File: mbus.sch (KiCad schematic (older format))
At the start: 17 parts, among them Q1 PN2222A, Q2 PN2222A, Q3 BC640, Q4 PN2222A

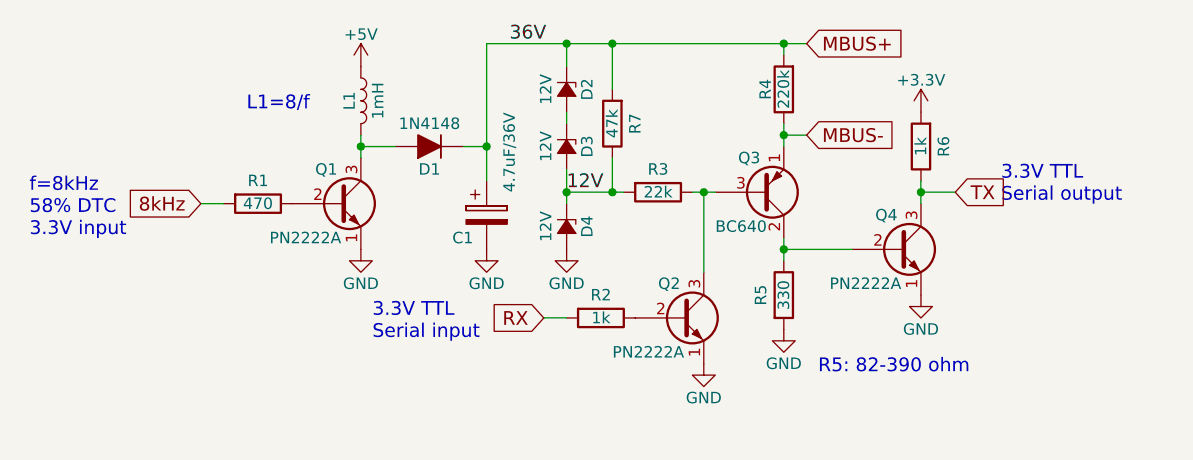
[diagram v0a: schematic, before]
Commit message: cosmetic changes (spacing)
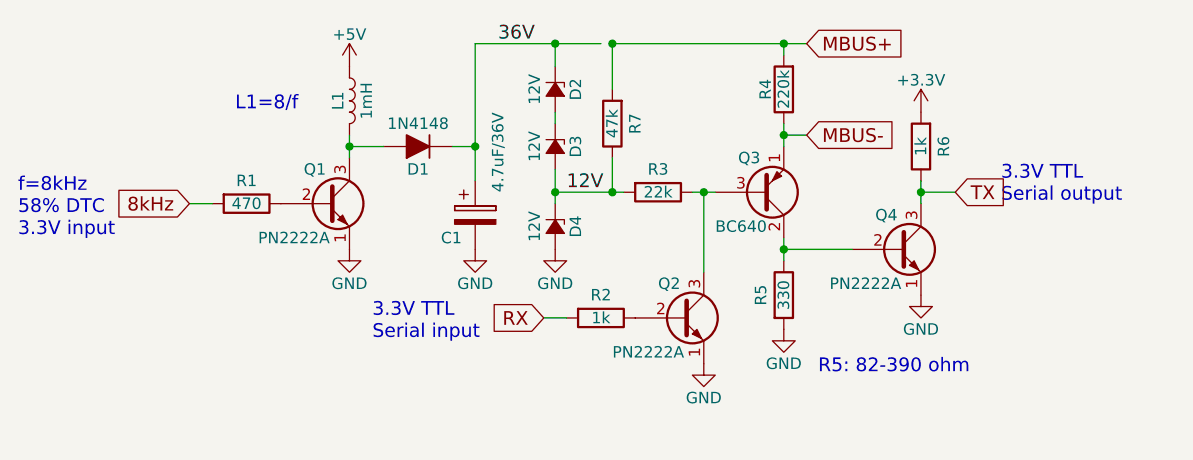
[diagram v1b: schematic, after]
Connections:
- wire segments 33 -> 23
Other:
- moved on the sheet: C1, D1, D2, D3, D4, L1, Q1, R1
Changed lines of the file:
@@
 L R R1
 U 1 1 59E32A7E
-P 2150 4300
-F 0 "R1" V 2050 4300 50  0000 C CNN
-F 1 "470" V 2150 4300 50  0000 C CNN
-F 2 "" V 2080 4300 50  0001 C CNN
-F 3 "" H 2150 4300 50  0001 C CNN
-	1    2150 4300
-	0    1    1    0
-$EndComp
-Wire Wire Line
-	2000 4300 1900 4300
+P 2100 4300
+F 0 "R1" V 2000 4300 50  0000 C CNN
+F 1 "470" V 2100 4300 50  0000 C CNN
+F 2 "" V 2030 4300 50  0001 C CNN
+F 3 "" H 2100 4300 50  0001 C CNN
+	1    2100 4300
+	0    1    1    0
+$EndComp
+Wire Wire Line
+	1950 4300 1850 4300
 $Comp
 L Q_NPN_EBC Q1
 U 1 1 59E32AF3
-P 2500 4300
-F 0 "Q1" H 2400 4450 50  0000 L CNN
-F 1 "PN2222A" H 2200 4150 50  0000 L CNN
-F 2 "" H 2700 4400 50  0001 C CNN
-F 3 "" H 2500 4300 50  0001 C CNN
-	1    2500 4300
+P 2450 4300
+F 0 "Q1" H 2350 4450 50  0000 L CNN
+F 1 "PN2222A" H 2150 4150 50  0000 L CNN
+F 2 "" H 2650 4400 50  0001 C CNN
+F 3 "" H 2450 4300 50  0001 C CNN
+	1    2450 4300
 	1    0    0    -1
 $EndComp
@@
 L GND #PWR2
 U 1 1 59E32B2F
-P 2600 4500
-F 0 "#PWR2" H 2600 4250 50  0001 C CNN
-F 1 "GND" H 2600 4350 50  0000 C CNN
-F 2 "" H 2600 4500 50  0001 C CNN
-F 3 "" H 2600 4500 50  0001 C CNN
-	1    2600 4500
+P 2550 4500
+F 0 "#PWR2" H 2550 4250 50  0001 C CNN
+F 1 "GND" H 2550 4350 50  0000 C CNN
+F 2 "" H 2550 4500 50  0001 C CNN
+F 3 "" H 2550 4500 50  0001 C CNN
+	1    2550 4500
 	1    0    0    -1
 $EndComp
@@
 L L L1
 U 1 1 59E32B47
-P 2600 3850
-F 0 "L1" V 2550 3850 50  0000 C CNN
-F 1 "1mH" V 2675 3850 50  0000 C CNN
-F 2 "" H 2600 3850 50  0001 C CNN
-F 3 "" H 2600 3850 50  0001 C CNN
-	1    2600 3850
-	1    0    0    -1
-$EndComp
-Wire Wire Line
-	2600 4000 2600 4050
-Wire Wire Line
-	2600 4050 2600 4100
+P 2550 3850
+F 0 "L1" V 2500 3850 50  0000 C CNN
+F 1 "1mH" V 2625 3850 50  0000 C CNN
+F 2 "" H 2550 3850 50  0001 C CNN
+F 3 "" H 2550 3850 50  0001 C CNN
+	1    2550 3850
+	1    0    0    -1
+$EndComp
+Wire Wire Line
+	2550 4000 2550 4100
 $Comp
 L +5V #PWR1
 U 1 1 59E32BAD
-P 2600 3700
-F 0 "#PWR1" H 2600 3550 50  0001 C CNN
-F 1 "+5V" H 2600 3840 50  0000 C CNN
-F 2 "" H 2600 3700 50  0001 C CNN
-F 3 "" H 2600 3700 50  0001 C CNN
-	1    2600 3700
+P 2550 3700
+F 0 "#PWR1" H 2550 3550 50  0001 C CNN
+F 1 "+5V" H 2550 3840 50  0000 C CNN
+F 2 "" H 2550 3700 50  0001 C CNN
+F 3 "" H 2550 3700 50  0001 C CNN
+	1    2550 3700
 	1    0    0    -1
 $EndComp
@@
 L D_ALT D1
 U 1 1 59E32BC7
-P 2900 4050
-F 0 "D1" H 2900 4150 50  0000 C CNN
-F 1 "1N4148" H 2900 3950 50  0000 C CNN
-F 2 "" H 2900 4050 50  0001 C CNN
-F 3 "" H 2900 4050 50  0001 C CNN
-	1    2900 4050
+P 2850 4050
+F 0 "D1" H 2850 4150 50  0000 C CNN
+F 1 "1N4148" H 2850 3950 50  0000 C CNN
+F 2 "" H 2850 4050 50  0001 C CNN
+F 3 "" H 2850 4050 50  0001 C CNN
+	1    2850 4050
 	-1   0    0    1
 $EndComp
 Wire Wire Line
-	2750 4050 2600 4050
-Connection ~ 2600 4050
+	2700 4050 2550 4050
+Connection ~ 2550 4050
 $Comp
 L D_Zener_Small_ALT D4
 U 1 1 59E32C36
-P 3500 4400
-F 0 "D4" H 3500 4490 50  0000 C CNN
-F 1 "12V" H 3500 4310 50  0000 C CNN
-F 2 "" V 3500 4400 50  0001 C CNN
-F 3 "" V 3500 4400 50  0001 C CNN
-	1    3500 4400
+P 3450 4400
+F 0 "D4" H 3450 4490 50  0000 C CNN
+F 1 "12V" H 3450 4310 50  0000 C CNN
+F 2 "" V 3450 4400 50  0001 C CNN
+F 3 "" V 3450 4400 50  0001 C CNN
+	1    3450 4400
 	0    1    1    0
 $EndComp
@@
 L D_Zener_Small_ALT D3
 U 1 1 59E32CBA
-P 3500 4050
-F 0 "D3" H 3500 4140 50  0000 C CNN
-F 1 "12V" H 3500 3960 50  0000 C CNN
-F 2 "" V 3500 4050 50  0001 C CNN
-F 3 "" V 3500 4050 50  0001 C CNN
-	1    3500 4050
+P 3450 4050
+F 0 "D3" H 3450 4140 50  0000 C CNN
+F 1 "12V" H 3450 3960 50  0000 C CNN
+F 2 "" V 3450 4050 50  0001 C CNN
+F 3 "" V 3450 4050 50  0001 C CNN
+	1    3450 4050
 	0    1    1    0
 $EndComp
@@
 L D_Zener_Small_ALT D2
 U 1 1 59E32D01
-P 3500 3800
-F 0 "D2" H 3500 3890 50  0000 C CNN
-F 1 "12V" H 3500 3710 50  0000 C CNN
-F 2 "" V 3500 3800 50  0001 C CNN
-F 3 "" V 3500 3800 50  0001 C CNN
-	1    3500 3800
+P 3450 3800
+F 0 "D2" H 3450 3890 50  0000 C CNN
+F 1 "12V" H 3450 3710 50  0000 C CNN
+F 2 "" V 3450 3800 50  0001 C CNN
+F 3 "" V 3450 3800 50  0001 C CNN
+	1    3450 3800
 	0    1    1    0
 $EndComp
@@
 L GND #PWR4
 U 1 1 59E32D8F
-P 3500 4500
-F 0 "#PWR4" H 3500 4250 50  0001 C CNN
-F 1 "GND" H 3500 4350 50  0000 C CNN
-F 2 "" H 3500 4500 50  0001 C CNN
-F 3 "" H 3500 4500 50  0001 C CNN
-	1    3500 4500
-	1    0    0    -1
-$EndComp
-Wire Wire Line
-	3500 4150 3500 4250
-Wire Wire Line
-	3500 4250 3500 4300
-Wire Wire Line
-	3500 3950 3500 3900
+P 3450 4500
+F 0 "#PWR4" H 3450 4250 50  0001 C CNN
+F 1 "GND" H 3450 4350 50  0000 C CNN
+F 2 "" H 3450 4500 50  0001 C CNN
+F 3 "" H 3450 4500 50  0001 C CNN
+	1    3450 4500
+	1    0    0    -1
+$EndComp
+Wire Wire Line
+	3450 4150 3450 4300
+Wire Wire Line
+	3450 3950 3450 3900
 $Comp
 L CP C1
 U 1 1 59E32EFA
-P 3150 4350
-F 0 "C1" H 3000 4250 50  0000 L CNN
-F 1 "4.7uF/36V" V 3250 4450 50  0000 L CNN
-F 2 "" H 3188 4200 50  0001 C CNN
-F 3 "" H 3150 4350 50  0001 C CNN
-	1    3150 4350
-	1    0    0    -1
-$EndComp
-Wire Wire Line
-	3150 3600 3150 4050
-Wire Wire Line
-	3150 4050 3150 4200
-Wire Wire Line
-	3150 3600 3500 3600
-Wire Wire Line
-	3500 3600 3700 3600
-Wire Wire Line
-	3700 3600 4450 3600
-Wire Wire Line
-	4450 3600 4550 3600
-Wire Wire Line
-	3500 3600 3500 3700
-Wire Wire Line
-	3050 4050 3150 4050
-Connection ~ 3150 4050
+P 3100 4350
+F 0 "C1" H 2950 4250 50  0000 L CNN
+F 1 "4.7uF/36V" V 3200 4450 50  0000 L CNN
+F 2 "" H 3138 4200 50  0001 C CNN
+F 3 "" H 3100 4350 50  0001 C CNN
+	1    3100 4350
+	1    0    0    -1
+$EndComp
+Wire Wire Line
+	3100 3600 3100 4200
+Wire Wire Line
+	3100 3600 3650 3600
+Wire Wire Line
+	3700 3600 4550 3600
+Wire Wire Line
+	3450 3600 3450 3700
+Wire Wire Line
+	3000 4050 3100 4050
+Connection ~ 3100 4050
 $Comp
 L GND #PWR3
 U 1 1 59E32FEB
-P 3150 4500
-F 0 "#PWR3" H 3150 4250 50  0001 C CNN
-F 1 "GND" H 3150 4350 50  0000 C CNN
-F 2 "" H 3150 4500 50  0001 C CNN
-F 3 "" H 3150 4500 50  0001 C CNN
-	1    3150 4500
+P 3100 4500
+F 0 "#PWR3" H 3100 4250 50  0001 C CNN
+F 1 "GND" H 3100 4350 50  0000 C CNN
+F 2 "" H 3100 4500 50  0001 C CNN
+F 3 "" H 3100 4500 50  0001 C CNN
+	1    3100 4500
 	1    0    0    -1
 $EndComp
@@
 $EndComp
 Wire Wire Line
-	3500 4250 3700 4250
-Wire Wire Line
-	3700 4250 3750 4250
-Connection ~ 3500 4250
+	3450 4250 3750 4250
+Connection ~ 3450 4250
 Text Label 3500 4250 0    60   ~ 0
 12V
-Text Label 3250 3600 0    60   ~ 0
+Text Label 3200 3600 0    60   ~ 0
 36V
 $Comp
@@
 $EndComp
 Wire Wire Line
-	4050 4250 4100 4250
-Wire Wire Line
-	4100 4250 4150 4250
+	4050 4250 4150 4250
 $Comp
 L Q_NPN_EBC Q2
@@
 Wire Wire Line
 	4450 3600 4450 3650
-Connection ~ 3500 3600
-Wire Wire Line
-	4450 3950 4450 4000
-Wire Wire Line
-	4450 4000 4450 4050
+Connection ~ 3450 3600
+Wire Wire Line
+	4450 3950 4450 4050
 $Comp
 L R R5
@@
 $EndComp
 Wire Wire Line
-	4450 4450 4450 4500
-Wire Wire Line
-	4450 4500 4450 4550
+	4450 4450 4450 4550
 $Comp
 L Q_NPN_EBC Q4
@@
 $EndComp
 Wire Wire Line
-	5050 4200 5050 4250
-Wire Wire Line
-	5050 4250 5050 4300
+	5050 4200 5050 4300
 Wire Wire Line
 	5050 4250 5200 4250
@@
 Text GLabel 5200 4250 2    60   Input ~ 0
 TX
-Text GLabel 1900 4300 0    60   Input ~ 0
+Text GLabel 1850 4300 0    60   Input ~ 0
 8kHz
 Text Notes 5400 4300 0    60   ~ 0
@@
 Text Notes 2650 4900 0    60   ~ 0
 3.3V TTL\nSerial input
-Text Notes 1150 4450 0    60   ~ 0
+Text Notes 1100 4450 0    60   ~ 0
 f=8kHz \n58% DTC\n3.3V input
 Text Notes 4600 5050 0    60   ~ 0
 R5: 82-390 ohm
-Text Notes 2100 3900 0    60   ~ 0
+Text Notes 2050 3900 0    60   ~ 0
 L1=8/f
 $Comp

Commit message: larger input resistor R2=15k
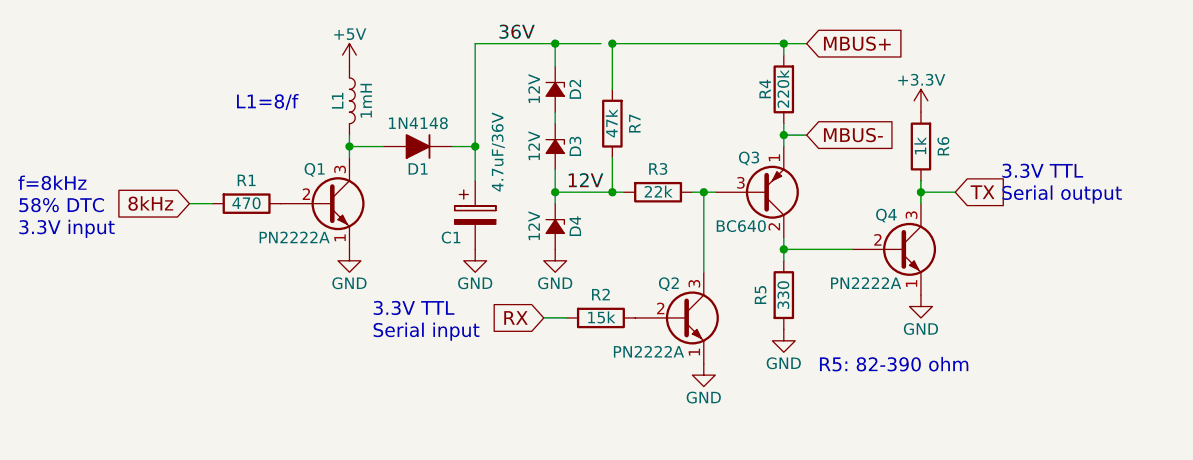
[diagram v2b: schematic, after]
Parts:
- R2: value 1k -> 15k
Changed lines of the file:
@@
 P 3650 4800
 F 0 "R2" V 3550 4800 50  0000 C CNN
-F 1 "1k" V 3650 4800 50  0000 C CNN
+F 1 "15k" V 3650 4800 50  0000 C CNN
 F 2 "" V 3580 4800 50  0001 C CNN
 F 3 "" H 3650 4800 50  0001 C CNN

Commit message: Pullup on RX and pic update
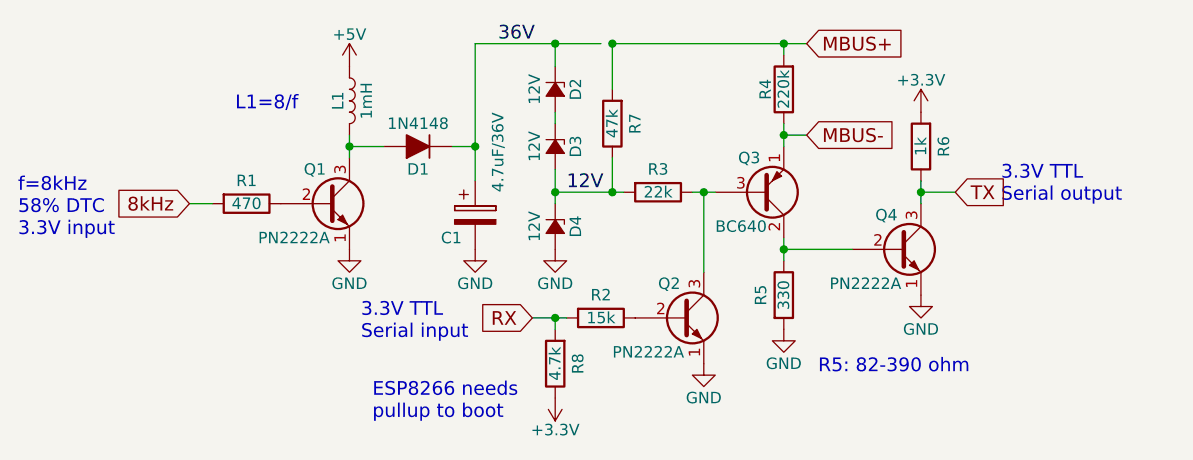
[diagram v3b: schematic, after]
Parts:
- added R8: 4.7k, symbol R
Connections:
- wire segments 23 -> 24
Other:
- note added: "ESP8266 needs\npullup to boot"
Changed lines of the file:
@@
 Connection ~ 4100 4250
 $Comp
-L GND #PWR5
+L GND #PWR6
 U 1 1 59E33748
 P 4100 5000
-F 0 "#PWR5" H 4100 4750 50  0001 C CNN
+F 0 "#PWR6" H 4100 4750 50  0001 C CNN
 F 1 "GND" H 4100 4850 50  0000 C CNN
 F 2 "" H 4100 5000 50  0001 C CNN
@@
 $EndComp
 Wire Wire Line
-	3500 4800 3400 4800
+	3500 4800 3350 4800
 $Comp
 L R R4
@@
 $EndComp
 $Comp
-L GND #PWR6
+L GND #PWR7
 U 1 1 59E33DF2
 P 4450 4850
-F 0 "#PWR6" H 4450 4600 50  0001 C CNN
+F 0 "#PWR7" H 4450 4600 50  0001 C CNN
 F 1 "GND" H 4450 4700 50  0000 C CNN
 F 2 "" H 4450 4850 50  0001 C CNN
@@
 Connection ~ 4450 4500
 $Comp
-L GND #PWR8
+L GND #PWR9
 U 1 1 59E34040
 P 5050 4700
-F 0 "#PWR8" H 5050 4450 50  0001 C CNN
+F 0 "#PWR9" H 5050 4450 50  0001 C CNN
 F 1 "GND" H 5050 4550 50  0000 C CNN
 F 2 "" H 5050 4700 50  0001 C CNN
@@
 	4450 4000 4550 4000
 Connection ~ 4450 4000
-Text GLabel 3400 4800 0    60   Input ~ 0
+Text GLabel 3350 4800 0    60   Input ~ 0
 RX
 Text GLabel 5200 4250 2    60   Input ~ 0
@@
 Text Notes 5400 4300 0    60   ~ 0
 3.3V TTL\nSerial output
-Text Notes 2650 4900 0    60   ~ 0
+Text Notes 2600 4900 0    60   ~ 0
 3.3V TTL\nSerial input
 Text Notes 1100 4450 0    60   ~ 0
@@
 L1=8/f
 $Comp
-L +3.3V #PWR?
+L +3.3V #PWR8
 U 1 1 59E48729
 P 5050 3900
-F 0 "#PWR?" H 5050 3750 50  0001 C CNN
+F 0 "#PWR8" H 5050 3750 50  0001 C CNN
 F 1 "+3.3V" H 5050 4040 50  0000 C CNN
 F 2 "" H 5050 3900 50  0001 C CNN
@@
 	1    0    0    -1
 $EndComp
+$Comp
+L R R8
+U 1 1 59E73425
+P 3450 5000
+F 0 "R8" V 3350 5000 50  0000 C CNN
+F 1 "4.7k" V 3450 5000 50  0000 C CNN
+F 2 "" V 3380 5000 50  0001 C CNN
+F 3 "" H 3450 5000 50  0001 C CNN
+	1    3450 5000
+	-1   0    0    1
+$EndComp
+Wire Wire Line
+	3450 4850 3450 4800
+Connection ~ 3450 4800
+$Comp
+L +3.3V #PWR5
+U 1 1 59E7355E
+P 3450 5150
+F 0 "#PWR5" H 3450 5000 50  0001 C CNN
+F 1 "+3.3V" H 3450 5290 50  0000 C CNN
+F 2 "" H 3450 5150 50  0001 C CNN
+F 3 "" H 3450 5150 50  0001 C CNN
+	1    3450 5150
+	-1   0    0    1
+$EndComp
+Text Notes 2650 5250 0    60   ~ 0
+ESP8266 needs\npullup to boot
 $EndSCHEMATC

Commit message: connect 36V line
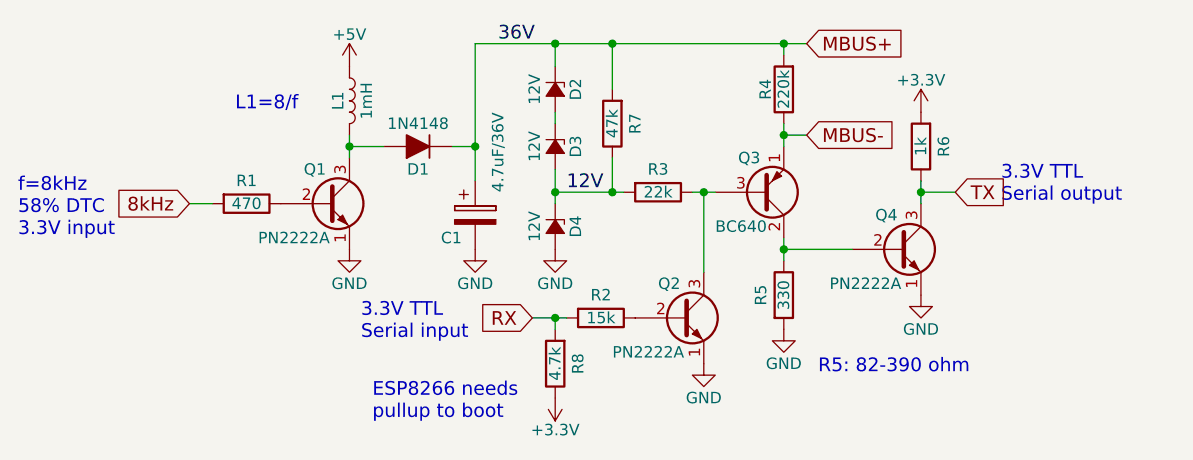
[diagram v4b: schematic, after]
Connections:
- wire segments 24 -> 23
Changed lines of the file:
@@
 	3100 3600 3100 4200
 Wire Wire Line
-	3100 3600 3650 3600
-Wire Wire Line
-	3700 3600 4550 3600
+	3100 3600 4550 3600
 Wire Wire Line
 	3450 3600 3450 3700
